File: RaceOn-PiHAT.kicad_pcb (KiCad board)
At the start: 2 copper layers, 65 x 56.5 mm, 66 parts, among them IC1 MIC29302WU, IC2 NCP5901B, IC3 NCP5901B, IC4 BD48K60G, IC5 LMR14030, J1 BATTERY, J2 ACCELEROMETER, J3 Pi Connector, J4 Encoder Left, J5 Encoder Right, M1 SERVO, M2 MOTOR, Q1 Si7288DP, Q2 Si7288DP, Q3 SQJA37EP1

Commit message: Version 2
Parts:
- removed C14: 47uF, Race On:CAPC320X250X270L60M
- removed C16: 47nF, Race On:CAPC200X125X95L45M
- removed C8: 1uF, Race On:CAPC200X125X95L45M
- removed FID1: Fiducial, Race On:FID1M3
- removed J4: Encoder Left, Race On:HDRV3W64P254_3X1_762X254H854
- removed J5: Encoder Right, Race On:HDRV3W64P254_3X1_762X254H854
- removed R11: 4.7k, Race On:RESC200X127X65L40M
- removed S1: LEFT, Race On:BTN4P450_600X900X350L83X70M
- removed S2: RIGHT, Race On:BTN4P450_600X900X350L83X70M
- removed TP1, TP2, TP3, TP4, TP5, TP6: TestPoint, Race On:TESTPOINT
- added D3: D, Race On:SOD350X160X120L45X62M, F.Cu at (148.5, 94.8)
- added IC10: SN74LVC2G07, Race On:SOT23-6P95_280X145L45X37M, F.Cu at (172.2, 72.8)
- added IC6: MPU-9250, Race On:PGA28P254C7R4L1840X1127H200, F.Cu at (172.3, 87.4)
- added IC7: SN74LVC2G07, Race On:SOT23-6P95_280X145L45X37M, F.Cu at (154.7, 79.8)
- added IC8: SN74LVC2G07, Race On:SOT23-6P95_280X145L45X37M, F.Cu at (154.7, 75.9)
- added IC9: SN74LVC2G07, Race On:SOT23-6P95_280X145L45X37M, F.Cu at (154.7, 83.7)
- added JP2: SolderJumper_2_Bridged, Jumper:SolderJumper-2_P1.3mm_Bridged_Pad1.0x1.5mm, B.Cu at (121.2, 93.3)
- added JP3: SolderJumper_2_Bridged, Jumper:SolderJumper-2_P1.3mm_Bridged_Pad1.0x1.5mm, B.Cu at (118.6, 93.3)
- added JP5: SolderJumper, Race On:SJ3B12P10X15, F.Cu at (161.2, 83.8)
- added L2: 1uH, Race On:INDM600X600X450L155X490M, F.Cu at (139.1, 102.1)
- added Q4: IPD50R380CE, Race On:DPAK3P460_990X239L160X76T650X546L, F.Cu at (136.4, 90.7)
- added Q5: IPD50R380CE, Race On:DPAK3P460_990X239L160X76T650X546L, F.Cu at (129.2, 90.7)
- added R13: 3.9k, Race On:RESC200X127X65L40M, F.Cu at (165.5, 72.2)
- added R14: 3.9k, Race On:RESC200X127X65L40M, F.Cu at (154.8, 72.8)
- added R15: 3.9k, Race On:RESC200X127X65L40M, F.Cu at (149.8, 84.6)
- added R16: 3.9k, Race On:RESC200X127X65L40M, F.Cu at (171.3, 77.3)
- added R17: 3.9k, Race On:RESC200X127X65L40M, F.Cu at (171.3, 79.8)
- added R18: 4.7k, Race On:RESC200X127X65L40M, F.Cu at (176.5, 71.3)
- added R19: 4.7k, Race On:RESC200X127X65L40M, F.Cu at (176.5, 74.4)
- added U1: CAT24C256, Race On:SOIC8P127_490X600X175L83X42M, F.Cu at (166.3, 77.4)
- added U5: SPX3819M5-L-1-8, Race On:SOT23-5P95_280X145L45X40M, F.Cu at (161.4, 75.3)
- C11: value 100uF -> 220uF
- C2: value 47nF -> 4.7uF; footprint Race On:CAPC200X125X95L45M -> Race On:CAPC320X160X180L50M
- C4: value 1uF -> 4.7uF; footprint Race On:CAPC200X125X95L45M -> Race On:CAPC320X160X180L50M
- C5: value 27nF -> 220uF; footprint Race On:CAPC200X125X95L45M -> Race On:CAPPM730X435X310L135X240L
- C7: value 47nF -> 100nF
- C9: value 1uF -> 100nF
- D1: value D_Schottky -> D; footprint Race On:DIOM795X590X261L117X305M -> Race On:SOD350X160X120L45X62M
- J2: value ACCELEROMETER -> Conn_02x03_Odd_Even; footprint Race On:HDRV4W64P254_4X1_1016X254H854 -> Race On:HDRV6W65P254_3X2_762X508H900
- L1: value 1uH -> 2.2uH
- LED3: value RED -> GREEN
- Q1, Q2: value Si7288DP -> IPD50R380CE; footprint Race On:ICSOFL8P127_515X615X112L61X42M -> Race On:DPAK3P460_990X239L160X76T650X546L
- R12: value 4.7k -> 3.9k
- R2, R3, R6: value 12.1k -> 3.9k
- R8: value 68.1k -> 64.9k
- moved C7 34.8 mm to (155.7, 108.2), turned to 180 degrees
- moved J2 27.6 mm to (179.9, 77.3), turned to 180 degrees
- moved C5 24.6 mm to (137.8, 109.1)
- moved C10 23.1 mm to (150.1, 76.9), turned to 270 degrees
- moved R5 21.9 mm to (179.9, 96.5), turned to 270 degrees
- moved IC4 19.8 mm to (162.2, 96.1), turned to 270 degrees
- moved C9 16.9 mm to (161.4, 78.8)
- moved R12 16.1 mm to (165.5, 69.8), turned to 180 degrees
- moved LS1 15.2 mm to (155.5, 91.0), turned to 0 degrees
- moved D1 12.6 mm to (141.5, 79.5), turned to 90 degrees
- moved LED4 12.2 mm to (179.4, 74.3)
- moved C2 11.8 mm to (143.9, 86.2), turned to 0 degrees
- moved Q2 11.2 mm to (129.2, 78.2), turned to 180 degrees
- moved C1 9.85 mm to (141.5, 74.7), turned to 270 degrees
- moved Q3 9.04 mm to (128.7, 107.9), turned to 180 degrees
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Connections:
- C10 pad 1: GND -> -VSW
- C10 pad 2: +BATT -> +VSW
- C11 pad 1: +BATT -> +VSW
- C11 pad 2: GND -> -VSW
- C2 pad 1: GND -> -VSW
- C2 pad 2: Net-(C1-Pad1) -> +VSW
- C5 pad 1: Net-(C5-Pad1) -> +BATT
- C5 pad 2: Net-(C1-Pad1) -> GND
- C6 pad 1: Net-(C5-Pad1) -> Net-(C6-Pad1)
- C7 pad 2: Net-(C5-Pad1) -> Net-(C7-Pad2)
- C9 pad 2: +BATT -> +1V8
- D1 pad 1: Net-(D1-Pad1) -> Net-(C1-Pad2)
- D1 pad 2: +5V -> +VSW
- IC2 pad 2: BCM22 -> Net-(IC2-Pad2)
- IC2 pad 3: BCM17 -> MOTOR_EN
- IC2 pad 4: +BATT -> +VSW
- IC2 pad 6: GND -> -VSW
- IC3 pad 2: BCM27 -> Net-(IC3-Pad2)
- IC3 pad 3: BCM17 -> MOTOR_EN
- IC3 pad 4: +BATT -> +VSW
- IC3 pad 6: GND -> -VSW
- IC3 pad 7: Net-(C5-Pad1) -> Net-(C6-Pad1)
- IC5 pad 6: Net-(C16-Pad2) -> Net-(C7-Pad2)
- J2 pad 2: GND -> +3V3
- J2 pad 3: BCM2 -> ENC_L
- J2 pad 4: BCM3 -> ENC_R
- J3 pad 1: Net-(D1-Pad1) -> +3V3
- J3 pad 10: GND -> BCM15
- J3 pad 11: BCM18 -> BCM17
- J3 pad 12: BCM17 -> BCM18
- J3 pad 13: GND -> BCM27
- J3 pad 14: BCM27 -> GND
- J3 pad 15: BCM23 -> BCM22
- J3 pad 16: BCM22 -> BCM23
- J3 pad 17: BCM24 -> +3V3
- J3 pad 18: +3V3 -> BCM24
- J3 pad 19: GND -> BCM10
- J3 pad 2: +3V3 -> +5V
- J3 pad 20: BCM10 -> GND
- J3 pad 21: BCM25 -> BCM9
- J3 pad 22: BCM9 -> BCM25
- J3 pad 23: BCM8 -> BCM11
- J3 pad 24: BCM11 -> BCM8
- J3 pad 25: BCM7 -> GND
- J3 pad 26: GND -> BCM7
- J3 pad 27: BCM1 -> BCM0
- J3 pad 28: BCM0 -> BCM1
- J3 pad 29: GND -> BCM5
- J3 pad 3: Net-(D1-Pad1) -> BCM2
- J3 pad 30: BCM5 -> GND
- J3 pad 31: BCM12 -> BCM6
- J3 pad 32: BCM6 -> BCM12
- J3 pad 33: GND -> BCM13
- J3 pad 34: BCM13 -> GND
- J3 pad 35: BCM16 -> BCM19
- J3 pad 36: BCM19 -> BCM16
- J3 pad 37: BCM20 -> BCM26
- J3 pad 38: BCM26 -> BCM20
- J3 pad 39: BCM21 -> GND
- J3 pad 4: BCM2 -> +5V
- J3 pad 40: GND -> BCM21
- J3 pad 5: GND -> BCM3
- J3 pad 6: BCM3 -> GND
- J3 pad 7: BCM14 -> BCM4
- J3 pad 8: BCM4 -> BCM14
- J3 pad 9: BCM15 -> GND
- LED1 pad 2: Net-(C3-Pad2) -> +5V
- LED3 pad 2: BCM16 -> +3V3
- LED4 pad 2: BCM26 -> +3V3
- LS1 pad 1: Net-(C3-Pad2) -> +5V
- M1 pad 1: BCM12 -> SERVO
- M2 pad 1: Net-(C1-Pad1) -> Net-(C6-Pad1)
- M2 pad 2: Net-(C5-Pad1) -> Net-(C1-Pad1)
- Q1 pad 1: Net-(C1-Pad1) -> Net-(IC2-Pad8)
- Q1 pad 2: Net-(IC2-Pad8) -> +VSW
- Q1 pad 3: GND -> Net-(C1-Pad1)
- Q2 pad 1: Net-(C5-Pad1) -> Net-(IC2-Pad5)
- Q2 pad 2: Net-(IC3-Pad8) -> Net-(C1-Pad1)
- Q2 pad 3: GND -> -VSW
- R12 pad 1: GND -> BCM0
- R12 pad 2: Net-(LED4-Pad1) -> VDD
- R2 pad 1: BCM13 -> SERVO
- R2 pad 2: BCM22 -> +5V
- R3 pad 1: GND -> MOTOR_EN
- R3 pad 2: BCM17 -> +5V
- R6 pad 1: BCM13 -> Net-(IC2-Pad2)
- R6 pad 2: BCM27 -> +5V
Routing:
- net +5V: track 50.9 -> 147.4 mm, vias 3 -> 8
- net VDD: track 0.00 -> 68.7 mm, vias 0 -> 2
- net SERVO: track 0.00 -> 61.0 mm, vias 0 -> 2
- net BCM12: track 76.8 -> 21.7 mm, vias 1 -> 0
- net BCM22: track 51.7 -> 0.00 mm, vias 3 -> 0
- net BCM27: track 51.3 -> 0.00 mm, vias 2 -> 0
- net +BATT: track 88.9 -> 39.1 mm, vias 14 -> 0
- net +3V3: track 51.5 -> 100.9 mm, vias 0 -> 2
- net BCM17: track 46.6 -> 0.00 mm, vias 3 -> 0
- net Net-(C3-Pad2): track 64.0 -> 18.5 mm, vias 3 -> 1
- net +VSW: track 0.00 -> 34.5 mm, vias 0 -> 20
- net BCM0: track 0.00 -> 32.1 mm
- net BCM24: track 29.4 -> 0.00 mm, vias 1 -> 0
- net Net-(C5-Pad1): track 28.7 -> 0.00 mm, vias 10 -> 0
- net Net-(IC3-Pad5): track 5.42 -> 33.1 mm
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- added copper zone on B.Cu, net +5V
- added copper zone on B.Cu, net +VSW
- added copper zone on F.Cu, net +VSW
- added copper zone on B.Cu, net -VSW
- added copper zone on F.Cu, net -VSW
- added copper zone on B.Cu, net Net-(C6-Pad1)
- added copper zone on F.Cu, net Net-(C6-Pad1)
- removed copper zone on B.Cu, net +BATT
- removed copper zone on B.Cu, net Net-(C5-Pad1)
- removed copper zone on F.Cu, net Net-(C5-Pad1)
- removed copper zone on B.Cu, net Net-(D1-Pad1)
- removed copper zone on F.Cu, net Net-(D1-Pad1)
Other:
- board text added: "+"
- board text added: "-"
- board text added: "1V8"
- board text added: "3V3"
- board text added: "5V"
- board text added: "6V"
- board text added: "L"
- board text added: "R"

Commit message: Production
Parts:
- removed M2: MOTOR, Race On:CON2P
- added C14: 220uF, Race On:CAPPM730X435X310L135X240L, F.Cu at (120.6, 74.2)
- added C16: 220uF, Race On:CAPPM730X435X310L135X240L, F.Cu at (120.6, 95.0)
- added C8: 47uF, Race On:CAPC320X250X270L60M, F.Cu at (159.1, 105.3)
- added J4: Screw_Terminal_01x02, TerminalBlock_Phoenix:TerminalBlock_Phoenix_PT-1,5-2-5.0-H_1x02_P5.00mm_Horizontal, F.Cu at (121.1, 82.1)
- added REF**: OSHW-Logo2_9.8x8mm_SilkScreen, Symbol:OSHW-Logo2_9.8x8mm_SilkScreen, F.Cu at (172.5, 87.4)
- J1: value BATTERY -> Screw_Terminal_01x02; footprint Race On:CON2P -> TerminalBlock_Phoenix:TerminalBlock_Phoenix_PT-1,5-2-5.0-H_1x02_P5.00mm_Horizontal
- R18, R19, R5, R7: value 4.7k -> 3.9k
- moved JP3 3.35 mm to (118.6, 96.7)
- moved JP4 3.35 mm to (121.2, 96.7)
- moved J1 2.15 mm to (121.1, 103.0)
- moved C7 1.97 mm to (154.9, 110.0), turned to 90 degrees
- moved R8 1.93 mm to (157.5, 110.0), turned to 270 degrees
- moved C15 1.08 mm to (155.4, 105.3), turned to 90 degrees
- renumbered JP5 to JP2, JP2 to JP4
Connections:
- net MOTOR_EN renamed DRV_EN
- J1 pad 1: Net-(J1-Pad1) -> GND
- J1 pad 2: GND -> Net-(J1-Pad2)
- Q3 pad 1: Net-(J1-Pad1) -> Net-(J1-Pad2)
- U5 pad 1: +5V -> +3V3
- U5 pad 3: +5V -> +3V3
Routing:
- net +3V3: track 100.9 -> 140.7 mm, vias 2 -> 4
- net +VSW: track 34.5 -> 68.9 mm
- net +5V: track 147.4 -> 122.0 mm, vias 8 -> 9
- net -VSW: track 10.8 -> 19.3 mm
- net GND: track 62.0 -> 69.4 mm, vias 52 -> 40
- net VFB: track 4.82 -> 8.43 mm
- net Net-(C7-Pad2): track 3.47 -> 4.33 mm
- added copper zone on F.Cu, net Net-(J1-Pad2)
- removed copper zone on F.Cu, net Net-(J1-Pad1)
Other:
- board text added: "0"
- board text added: "1"
- board text added: "10"
- board text added: "11"
- board text added: "12"
- board text added: "13"
- board text added: "14"
- board text added: "15"
- board text added: "16"
- board text added: "17"
- board text added: "18"
- board text added: "19"
- board text added: "2"
- board text added: "20"
- board text added: "21"
- board text added: "22"
- board text added: "23"
- board text added: "24"
- board text added: "25"
- board text added: "26"
- board text added: "27"
- board text added: "3"
- board text added: "4"
- board text added: "5"
- board text added: "6"
- board text added: "7"
- board text added: "8"
- board text added: "9"
- board text added: "GND"
- board text added: "SCL"
- board text added: "SDA"
- board text added: "V 1.2"
- board text added: "VIO"

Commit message: Partial fix
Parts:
- removed C14, C16: 220uF, Race On:CAPPM730X435X310L135X240L
- removed C9: 100nF, Race On:CAPC200X125X95L45M
- removed IC10: SN74LVC2G07, Race On:SOT23-6P95_280X145L45X37M
- removed L2: 1uH, Race On:INDM600X600X450L155X490M
- removed R16, R17: 3.9k, Race On:RESC200X127X65L40M
- removed REF**: OSHW-Logo2_9.8x8mm_SilkScreen, Symbol:OSHW-Logo2_9.8x8mm_SilkScreen
- removed U5: SPX3819M5-L-1-8, Race On:SOT23-5P95_280X145L45X40M
- added JP5: SolderJumper_2_Bridged, Jumper:SolderJumper-2_P1.3mm_Bridged_Pad1.0x1.5mm, F.Cu at (138.2, 102.5)
- JP2: value SolderJumper -> SolderJumper_2_Bridged; footprint Race On:SJ3B12P10X15 -> Jumper:SolderJumper-2_P1.3mm_Bridged_Pad1.0x1.5mm
- LOGO1: footprint Race On:RACEON-LOGO -> Race On:RACEON
- moved JP2 27.7 mm to (140.7, 102.5)
- moved J4 6.60 mm to (121.3, 75.5)
- moved U1 3.75 mm to (163.5, 74.9), turned to 270 degrees
- moved R12 3.58 mm to (168.7, 71.4), turned to 270 degrees
- moved J1 3.50 mm to (121.2, 99.5)
- moved M1 1.85 mm to (180.1, 108.2)
- moved JP1 1.60 mm to (177.6, 105.6)
- moved R13 1.50 mm to (165.5, 70.7), turned to 0 degrees
- moved LED1 1.40 mm to (173.0, 116.9)
- moved LED2 1.40 mm to (165.8, 116.9)
- moved R7 1.40 mm to (169.3, 116.8)
- moved LOGO1 1.17 mm to (142.6, 115.2)
- moved LS1 0.45 mm to (155.1, 90.8)
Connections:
- IC6 pad 8: VDD -> Net-(IC6-Pad8)
- IC7 pad 5: VDD -> +3V3
- IC8 pad 5: VDD -> +3V3
- IC9 pad 5: VDD -> +3V3
- J2 pad 3: ENC_L -> BCM16
- J2 pad 4: ENC_R -> BCM26
- JP2 pad 1: +3V3 -> +BATT
- JP2 pad 2: VDD -> +VSW
- R12 pad 2: VDD -> +3V3
- R13 pad 2: VDD -> +3V3
- R18 pad 1: ENC_L -> BCM16
- R19 pad 1: ENC_R -> BCM26
- U1 pad 8: VDD -> +3V3
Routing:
- net VDD: track 68.7 -> 0.00 mm, vias 2 -> 0
- net +VSW: track 68.9 -> 34.5 mm
- net +3V3: track 140.7 -> 122.8 mm, vias 4 -> 2
- net GND: track 69.4 -> 56.6 mm, vias 40 -> 37
- net BCM0: track 32.1 -> 42.0 mm, vias 0 -> 2
- net ENC_L: track 9.29 -> 0.00 mm
- net ENC_R: track 8.53 -> 0.00 mm
- net +1V8: track 6.46 -> 0.00 mm
- net Net-(LED1-Pad1): track 21.8 -> 27.3 mm
- net +5V: track 122.0 -> 125.6 mm
- net BCM16: track 20.8 -> 23.7 mm
- net Net-(C3-Pad2): track 18.5 -> 19.8 mm
- net BCM26: track 17.2 -> 16.9 mm, vias 2 -> 0
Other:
- board text added: "BATTERY"
- board text added: "LOW BAT"
- board text added: "MOTOR"
- board text added: "V 1.3"
- board text added: "s"
- board text removed: "1V8"
- board text removed: "LOW BATT"
- board text removed: "V 1.2"
- board text removed: "VIO"

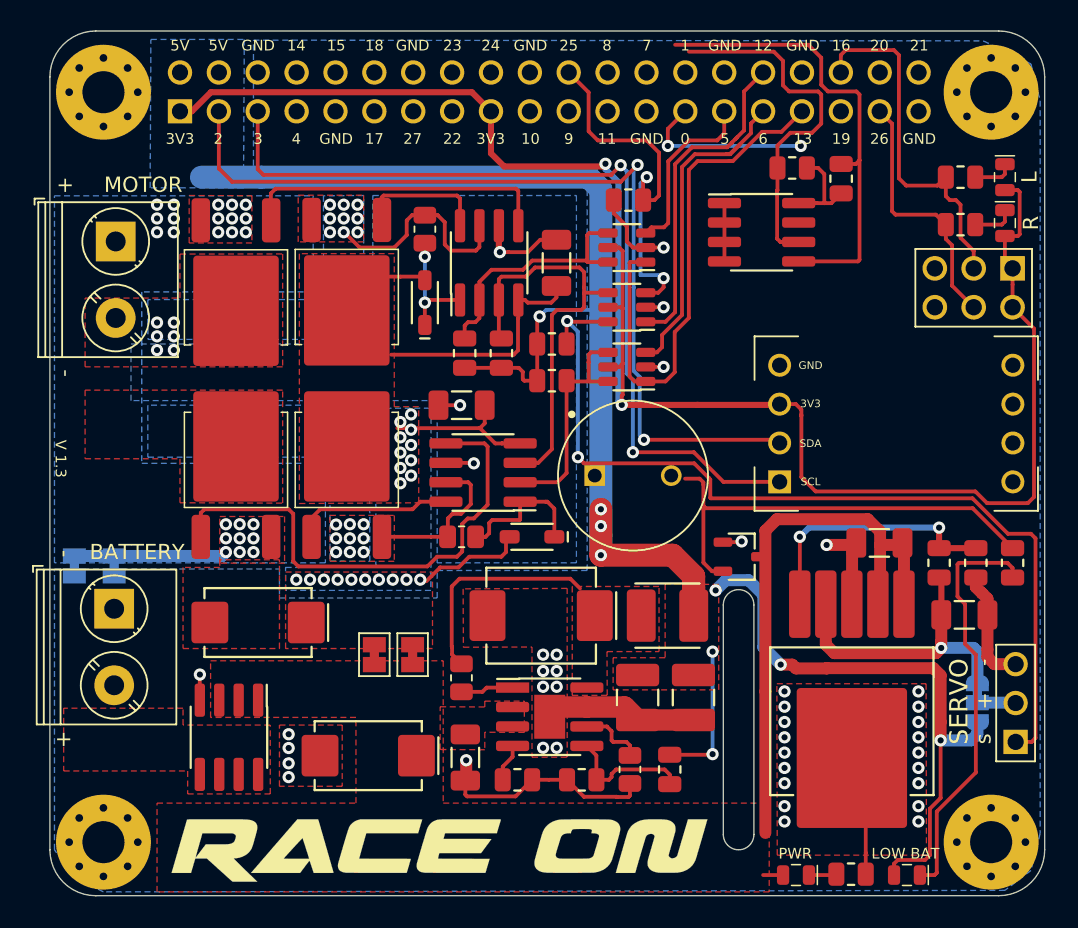
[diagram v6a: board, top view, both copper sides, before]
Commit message: Reverded to production board
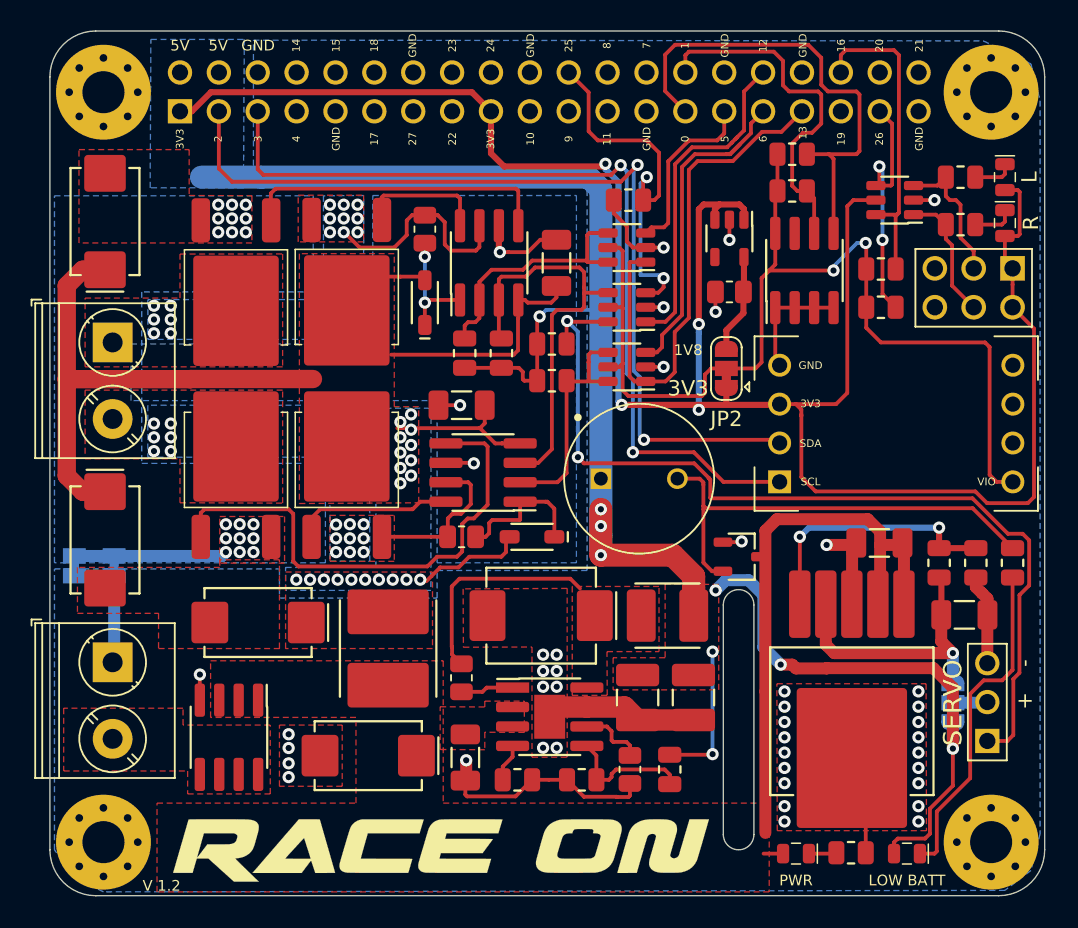
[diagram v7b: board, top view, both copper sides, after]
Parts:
- removed JP5: SolderJumper_2_Bridged, Jumper:SolderJumper-2_P1.3mm_Bridged_Pad1.0x1.5mm
- added C14: 220uF, Race On:CAPPM730X435X310L135X240L, F.Cu at (120.6, 74.2)
- added C16: 220uF, Race On:CAPPM730X435X310L135X240L, F.Cu at (120.6, 95.0)
- added C9: 100nF, Race On:CAPC200X125X95L45M, F.Cu at (161.4, 78.8)
- added IC10: SN74LVC2G07, Race On:SOT23-6P95_280X145L45X37M, F.Cu at (172.2, 72.8)
- added L2: 1uH, Race On:INDM600X600X450L155X490M, F.Cu at (139.1, 102.1)
- added R16: 3.9k, Race On:RESC200X127X65L40M, F.Cu at (171.3, 77.3)
- added R17: 3.9k, Race On:RESC200X127X65L40M, F.Cu at (171.3, 79.8)
- added U5: SPX3819M5-L-1-8, Race On:SOT23-5P95_280X145L45X40M, F.Cu at (161.4, 75.3)
- JP2: value SolderJumper_2_Bridged -> SolderJumper; footprint Jumper:SolderJumper-2_P1.3mm_Bridged_Pad1.0x1.5mm -> Race On:SJ3B12P10X15
- moved JP2 27.7 mm to (161.2, 83.8)
- moved J4 6.60 mm to (121.1, 82.1)
- moved U1 3.75 mm to (166.3, 77.4), turned to 0 degrees
- moved R12 3.58 mm to (165.5, 69.8), turned to 180 degrees
- moved J1 3.50 mm to (121.1, 103.0)
- moved M1 1.85 mm to (178.2, 108.1)
- moved JP1 1.60 mm to (176.0, 105.6)
- moved R13 1.50 mm to (165.5, 72.2), turned to 180 degrees
- moved LED1 1.40 mm to (173.0, 115.5)
- moved LED2 1.40 mm to (165.8, 115.5)
- moved R7 1.40 mm to (169.3, 115.4)
- moved LS1 0.45 mm to (155.5, 91.0)
- moved LOGO1 0.10 mm to (142.7, 115.2)
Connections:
- IC6 pad 8: Net-(IC6-Pad8) -> VDD
- IC7 pad 5: +3V3 -> VDD
- IC8 pad 5: +3V3 -> VDD
- IC9 pad 5: +3V3 -> VDD
- J2 pad 3: BCM16 -> ENC_L
- J2 pad 4: BCM26 -> ENC_R
- JP2 pad 1: +BATT -> +3V3
- JP2 pad 2: +VSW -> VDD
- R12 pad 2: +3V3 -> VDD
- R13 pad 2: +3V3 -> VDD
- R18 pad 1: BCM16 -> ENC_L
- R19 pad 1: BCM26 -> ENC_R
- U1 pad 8: +3V3 -> VDD
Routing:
- net VDD: track 0.00 -> 68.7 mm, vias 0 -> 2
- net +VSW: track 34.5 -> 68.9 mm
- net +3V3: track 122.8 -> 140.7 mm, vias 2 -> 4
- net GND: track 56.6 -> 69.4 mm, vias 37 -> 40
- net BCM0: track 42.0 -> 32.1 mm, vias 2 -> 0
- net ENC_L: track 0.00 -> 9.29 mm
- net ENC_R: track 0.00 -> 8.53 mm
- net +1V8: track 0.00 -> 6.46 mm
- net Net-(LED1-Pad1): track 27.3 -> 21.8 mm
- net +5V: track 125.6 -> 122.0 mm
- net BCM16: track 23.7 -> 20.8 mm
- net Net-(C3-Pad2): track 19.8 -> 18.5 mm
- net BCM26: track 16.9 -> 17.2 mm, vias 0 -> 2
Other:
- board text added: "1V8"
- board text added: "LOW BATT"
- board text added: "V 1.2"
- board text added: "VIO"
- board text removed: "BATTERY"
- board text removed: "LOW BAT"
- board text removed: "MOTOR"
- board text removed: "V 1.3"
- board text removed: "s"
